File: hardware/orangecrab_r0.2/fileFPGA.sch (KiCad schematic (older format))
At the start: 11 parts, among them J6 JTAG, U3 ECP5U25, U6 AT25SF081

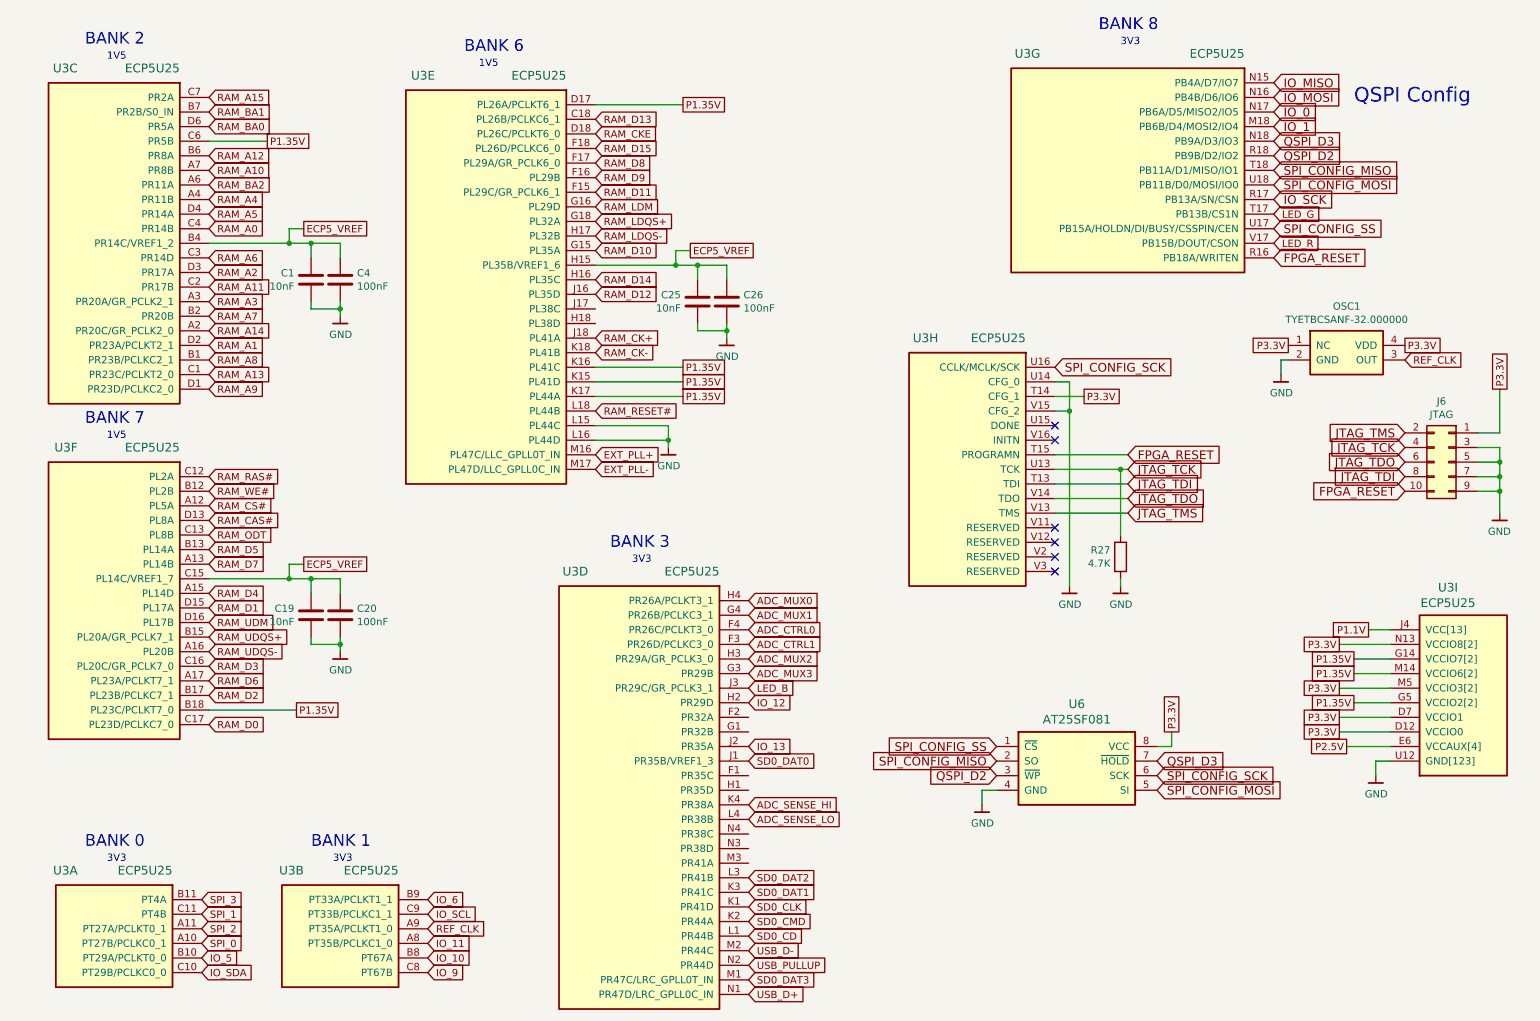
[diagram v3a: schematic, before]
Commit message: hw: Update board with 3d models Finish pin-swaps and routing of open changes General cleanups
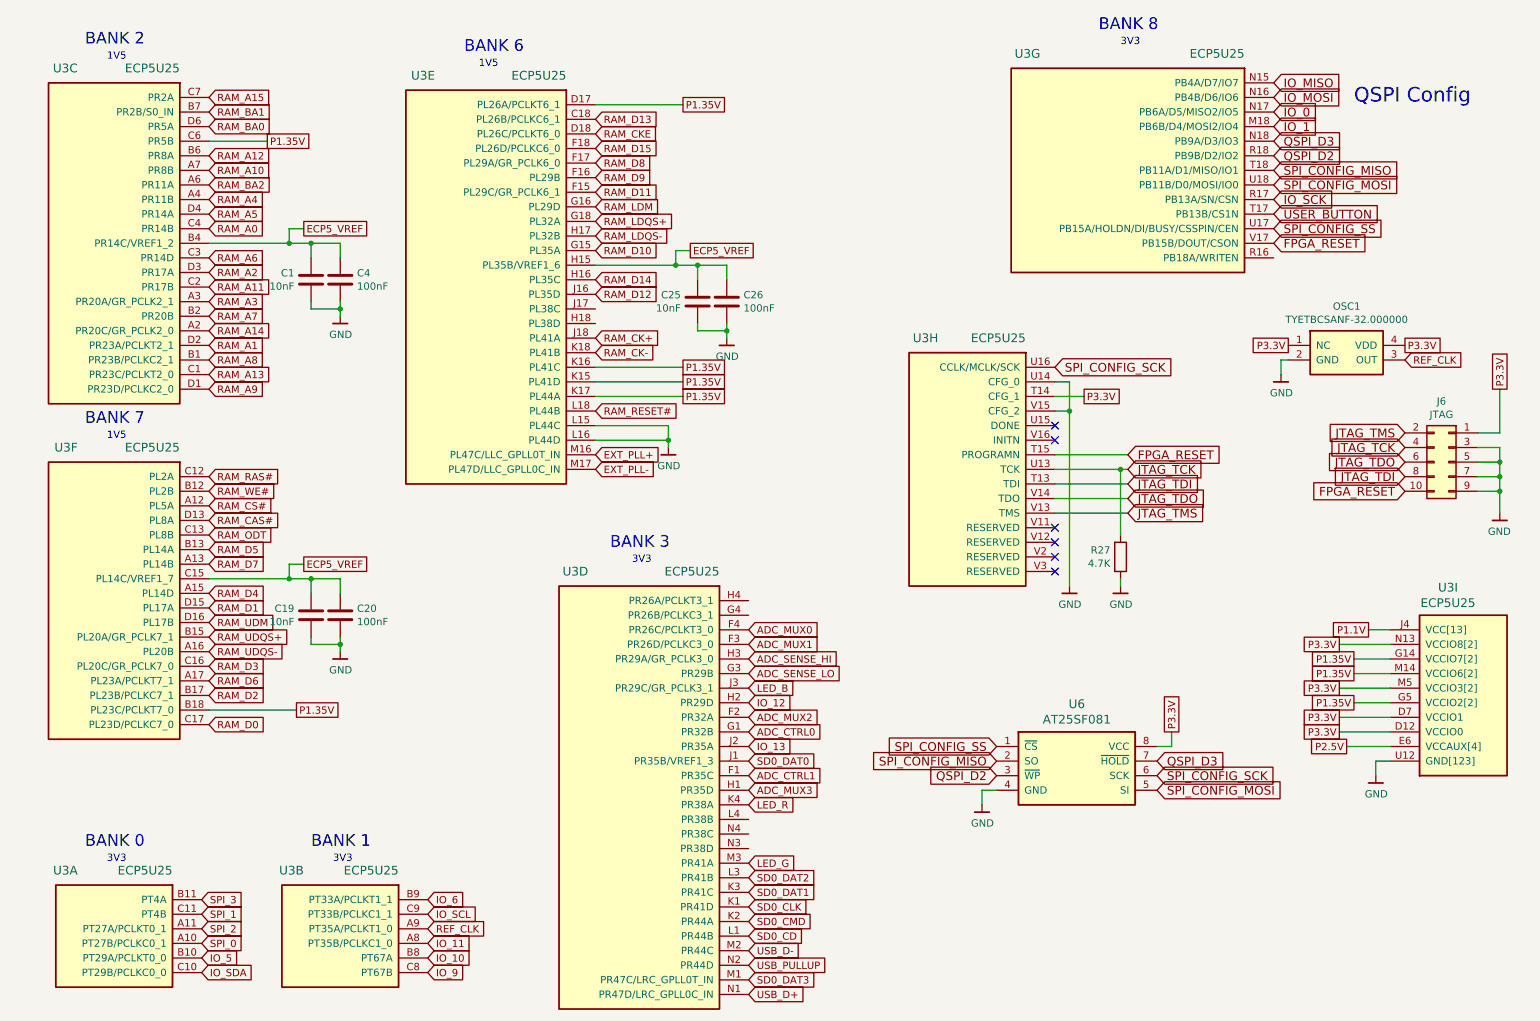
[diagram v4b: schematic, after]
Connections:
- net ADC_CTRL0: now also U3.G1 (PR32B); no longer U3.F4 (PR26C/PCLKT3_0)
- net ADC_CTRL1: now also U3.F1 (PR35C); no longer U3.F3 (PR26D/PCLKC3_0)
- net ADC_MUX0: now also U3.F4 (PR26C/PCLKT3_0); no longer U3.H4 (PR26A/PCLKT3_1)
- net ADC_MUX1: now also U3.F3 (PR26D/PCLKC3_0); no longer U3.G4 (PR26B/PCLKC3_1)
- net ADC_MUX2: now also U3.F2 (PR32A); no longer U3.H3 (PR29A/GR_PCLK3_0)
- net ADC_MUX3: now also U3.H1 (PR35D); no longer U3.G3 (PR29B)
- net ADC_SENSE_HI: now also U3.H3 (PR29A/GR_PCLK3_0); no longer U3.K4 (PR38A)
- net ADC_SENSE_LO: now also U3.G3 (PR29B); no longer U3.L4 (PR38B)
- net FPGA_RESET: now also U3.V17 (PB15B/DOUT/CSON); no longer U3.R16 (PB18A/WRITEN)
- net LED_G: now also U3.M3 (PR41A); no longer U3.T17 (PB13B/CS1N)
- net LED_R: now also U3.K4 (PR38A); no longer U3.V17 (PB15B/DOUT/CSON)
- new net USER_BUTTON: U3.T17 (PB13B/CS1N)
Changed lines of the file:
@@
 Text Notes 1300 3600 0    50   ~ 0
 1V5
-Text GLabel 9300 2350 2    60   Input ~ 0
+Text GLabel 9300 2250 2    60   Input ~ 0
 FPGA_RESET
 Text GLabel 8300 4100 2    60   Input ~ 0
@@
 Text GLabel 1950 7250 2    50   Input ~ 0
 IO_SDA
-Text GLabel 9300 2250 2    50   Input ~ 0
+Text GLabel 5700 6100 2    50   Input ~ 0
 LED_R
-Text GLabel 9300 2050 2    50   Input ~ 0
+Text GLabel 5700 6500 2    50   Input ~ 0
 LED_G
 Text GLabel 5700 5300 2    50   Input ~ 0
@@
 Text GLabel 2000 1250 2    50   Input ~ 0
 RAM_A15
-Text GLabel 5700 4700 2    50   Input ~ 0
+Text GLabel 5700 4900 2    50   Input ~ 0
 ADC_MUX0
-Text GLabel 5700 4800 2    50   Input ~ 0
+Text GLabel 5700 5000 2    50   Input ~ 0
 ADC_MUX1
+Text GLabel 5700 5500 2    50   Input ~ 0
+ADC_MUX2
+Text GLabel 5700 6000 2    50   Input ~ 0
+ADC_MUX3
+Text GLabel 5700 5900 2    50   Input ~ 0
+ADC_CTRL1
+Text GLabel 5700 5200 2    50   Input ~ 0
+ADC_SENSE_LO
 Text GLabel 5700 5100 2    50   Input ~ 0
-ADC_MUX2
-Text GLabel 5700 5200 2    50   Input ~ 0
-ADC_MUX3
-Text GLabel 5700 5000 2    50   Input ~ 0
-ADC_CTRL1
-Text GLabel 5700 6200 2    50   Input ~ 0
-ADC_SENSE_LO
-Text GLabel 5700 6100 2    50   Input ~ 0
 ADC_SENSE_HI
-Text GLabel 5700 4900 2    50   Input ~ 0
+Text GLabel 5700 5600 2    50   Input ~ 0
 ADC_CTRL0
+Text GLabel 9300 2050 2    60   Input ~ 0
+USER_BUTTON
 $EndSCHEMATC

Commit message: hw: Route last FPGA I/O to A[0-5]
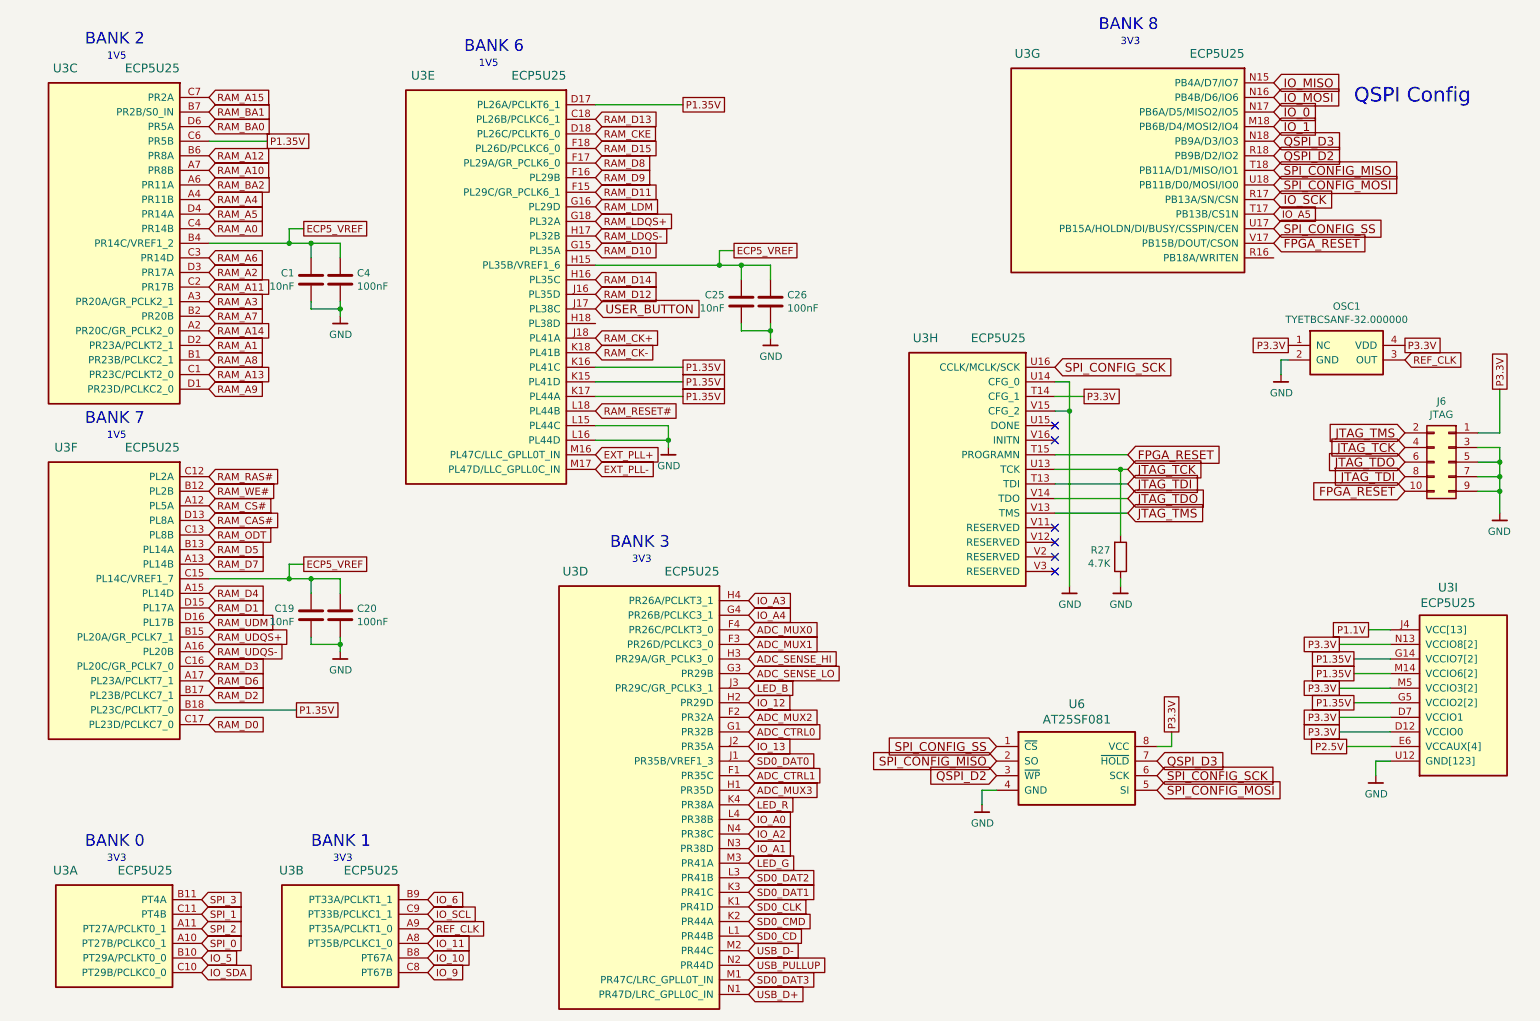
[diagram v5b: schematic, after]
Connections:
- net USER_BUTTON: now also U3.J17 (PL38C); no longer U3.T17 (PB13B/CS1N)
- net IO_A4: now reaches U3.G4 (PR26B/PCLKC3_1)
- net IO_A3: now reaches U3.H4 (PR26A/PCLKT3_1)
- net IO_A0: now reaches U3.L4 (PR38B)
- net IO_A1: now reaches U3.N3 (PR38D)
- net IO_A2: now reaches U3.N4 (PR38C)
- new net IO_A5: U3.T17 (PB13B/CS1N)
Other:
- moved on the sheet: C25, C26
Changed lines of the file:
@@
 L Device:C C25
 U 1 1 5D84AAF2
-P 5350 2650
-F 0 "C25" H 5235 2696 50  0000 R CNN
-F 1 "10nF" H 5235 2605 50  0000 R CNN
-F 2 "Capacitor_SMD:C_0201_0603Metric" H 5388 2500 50  0001 C CNN
-F 3 "~" H 5350 2650 50  0001 C CNN
-F 4 "Samsung Electro-Mechanics" H 5350 2650 50  0001 C CNN "Mfg"
-F 5 "CL03B103KP3NNNC" H 5350 2650 50  0001 C CNN "PN"
-	1    5350 2650
+P 5650 2650
+F 0 "C25" H 5535 2696 50  0000 R CNN
+F 1 "10nF" H 5535 2605 50  0000 R CNN
+F 2 "Capacitor_SMD:C_0201_0603Metric" H 5688 2500 50  0001 C CNN
+F 3 "~" H 5650 2650 50  0001 C CNN
+F 4 "Samsung Electro-Mechanics" H 5650 2650 50  0001 C CNN "Mfg"
+F 5 "CL03B103KP3NNNC" H 5650 2650 50  0001 C CNN "PN"
+	1    5650 2650
 	1    0    0    -1
 $EndComp
@@
 L Device:C C26
 U 1 1 5D84AAFC
-P 5550 2650
-F 0 "C26" H 5665 2696 50  0000 L CNN
-F 1 "100nF" H 5665 2605 50  0000 L CNN
-F 2 "Capacitor_SMD:C_0201_0603Metric" H 5588 2500 50  0001 C CNN
-F 3 "~" H 5550 2650 50  0001 C CNN
-F 4 "Samsung Electro-Mechanics" H 5550 2650 50  0001 C CNN "Mfg"
-F 5 "CL03A104KQ3NNNC" H 5550 2650 50  0001 C CNN "PN"
-	1    5550 2650
+P 5850 2650
+F 0 "C26" H 5965 2696 50  0000 L CNN
+F 1 "100nF" H 5965 2605 50  0000 L CNN
+F 2 "Capacitor_SMD:C_0201_0603Metric" H 5888 2500 50  0001 C CNN
+F 3 "~" H 5850 2650 50  0001 C CNN
+F 4 "Samsung Electro-Mechanics" H 5850 2650 50  0001 C CNN "Mfg"
+F 5 "CL03A104KQ3NNNC" H 5850 2650 50  0001 C CNN "PN"
+	1    5850 2650
 	1    0    0    -1
 $EndComp
@@
 L gkl_power:GND #PWR0130
 U 1 1 5D84AB06
-P 5550 2900
-F 0 "#PWR0130" H 5550 2650 50  0001 C CNN
-F 1 "GND" H 5553 2774 50  0000 C CNN
-F 2 "" H 5450 2550 50  0001 C CNN
-F 3 "" H 5550 2900 50  0001 C CNN
-	1    5550 2900
-	1    0    0    -1
-$EndComp
-Text GLabel 5300 2300 2    50   UnSpc ~ 0
+P 5850 2900
+F 0 "#PWR0130" H 5850 2650 50  0001 C CNN
+F 1 "GND" H 5853 2774 50  0000 C CNN
+F 2 "" H 5750 2550 50  0001 C CNN
+F 3 "" H 5850 2900 50  0001 C CNN
+	1    5850 2900
+	1    0    0    -1
+$EndComp
+Text GLabel 5600 2300 2    50   UnSpc ~ 0
 ECP5_VREF
 Wire Wire Line
-	4650 2400 5200 2400
-Wire Wire Line
-	5200 2400 5200 2300
-Wire Wire Line
-	5200 2300 5300 2300
-Wire Wire Line
-	5200 2400 5350 2400
-Wire Wire Line
-	5350 2400 5350 2500
-Connection ~ 5200 2400
-Wire Wire Line
-	5350 2400 5550 2400
-Wire Wire Line
-	5550 2400 5550 2500
-Connection ~ 5350 2400
-Wire Wire Line
-	5550 2800 5550 2850
-Wire Wire Line
-	5350 2800 5350 2850
-Wire Wire Line
-	5350 2850 5550 2850
-Connection ~ 5550 2850
-Wire Wire Line
-	5550 2850 5550 2900
+	4650 2400 5500 2400
+Wire Wire Line
+	5500 2400 5500 2300
+Wire Wire Line
+	5500 2300 5600 2300
+Wire Wire Line
+	5500 2400 5650 2400
+Wire Wire Line
+	5650 2400 5650 2500
+Connection ~ 5500 2400
+Wire Wire Line
+	5650 2400 5850 2400
+Wire Wire Line
+	5850 2400 5850 2500
+Connection ~ 5650 2400
+Wire Wire Line
+	5850 2800 5850 2850
+Wire Wire Line
+	5650 2800 5650 2850
+Wire Wire Line
+	5650 2850 5850 2850
+Connection ~ 5850 2850
+Wire Wire Line
+	5850 2850 5850 2900
 Text GLabel 9850 5100 0    50   UnSpc ~ 0
 P1.35V
@@
 Text GLabel 5700 5600 2    50   Input ~ 0
 ADC_CTRL0
-Text GLabel 9300 2050 2    60   Input ~ 0
+Text GLabel 4650 2700 2    60   Input ~ 0
 USER_BUTTON
+Text GLabel 9300 2050 2    50   Input ~ 0
+IO_A5
+Text GLabel 5700 6200 2    50   Input ~ 0
+IO_A0
+Text GLabel 5700 6400 2    50   Input ~ 0
+IO_A1
+Text GLabel 5700 6300 2    50   Input ~ 0
+IO_A2
+Text GLabel 5700 4700 2    50   Input ~ 0
+IO_A3
+Text GLabel 5700 4800 2    50   Input ~ 0
+IO_A4
 $EndSCHEMATC
